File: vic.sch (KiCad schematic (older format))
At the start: 16 parts, among them U19 2016, U20 4066, U21 8564, U29 7406, U56 74LS74

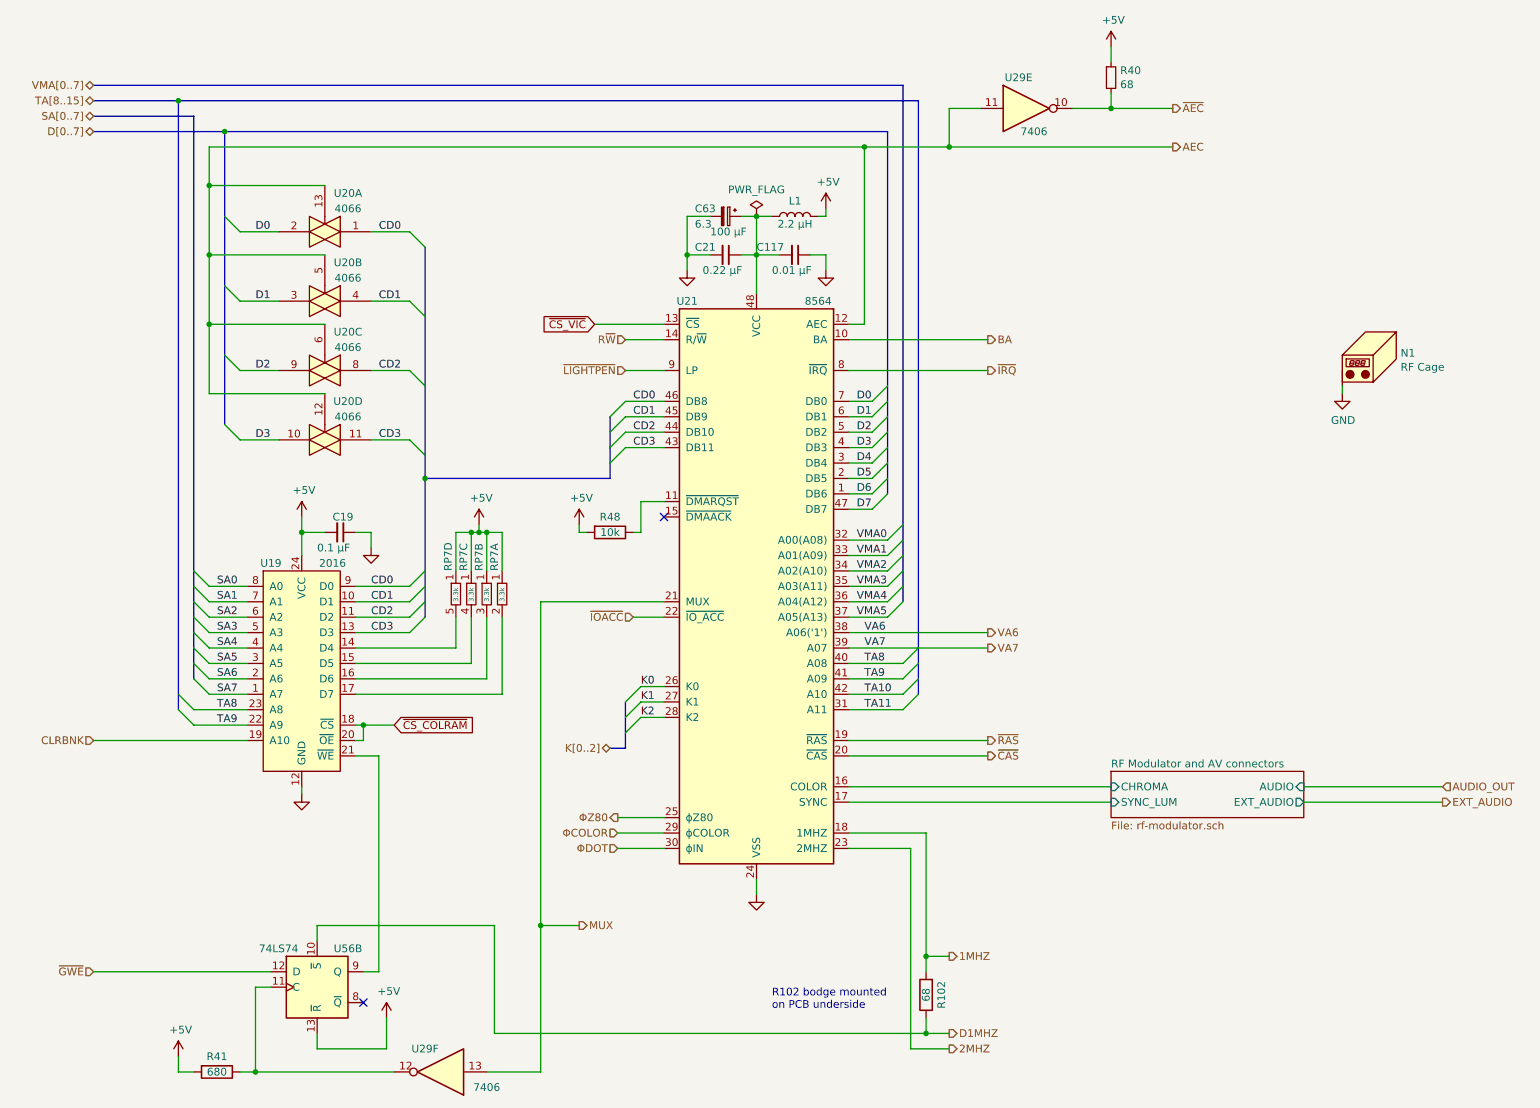
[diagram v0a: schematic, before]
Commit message: Clean up schematic
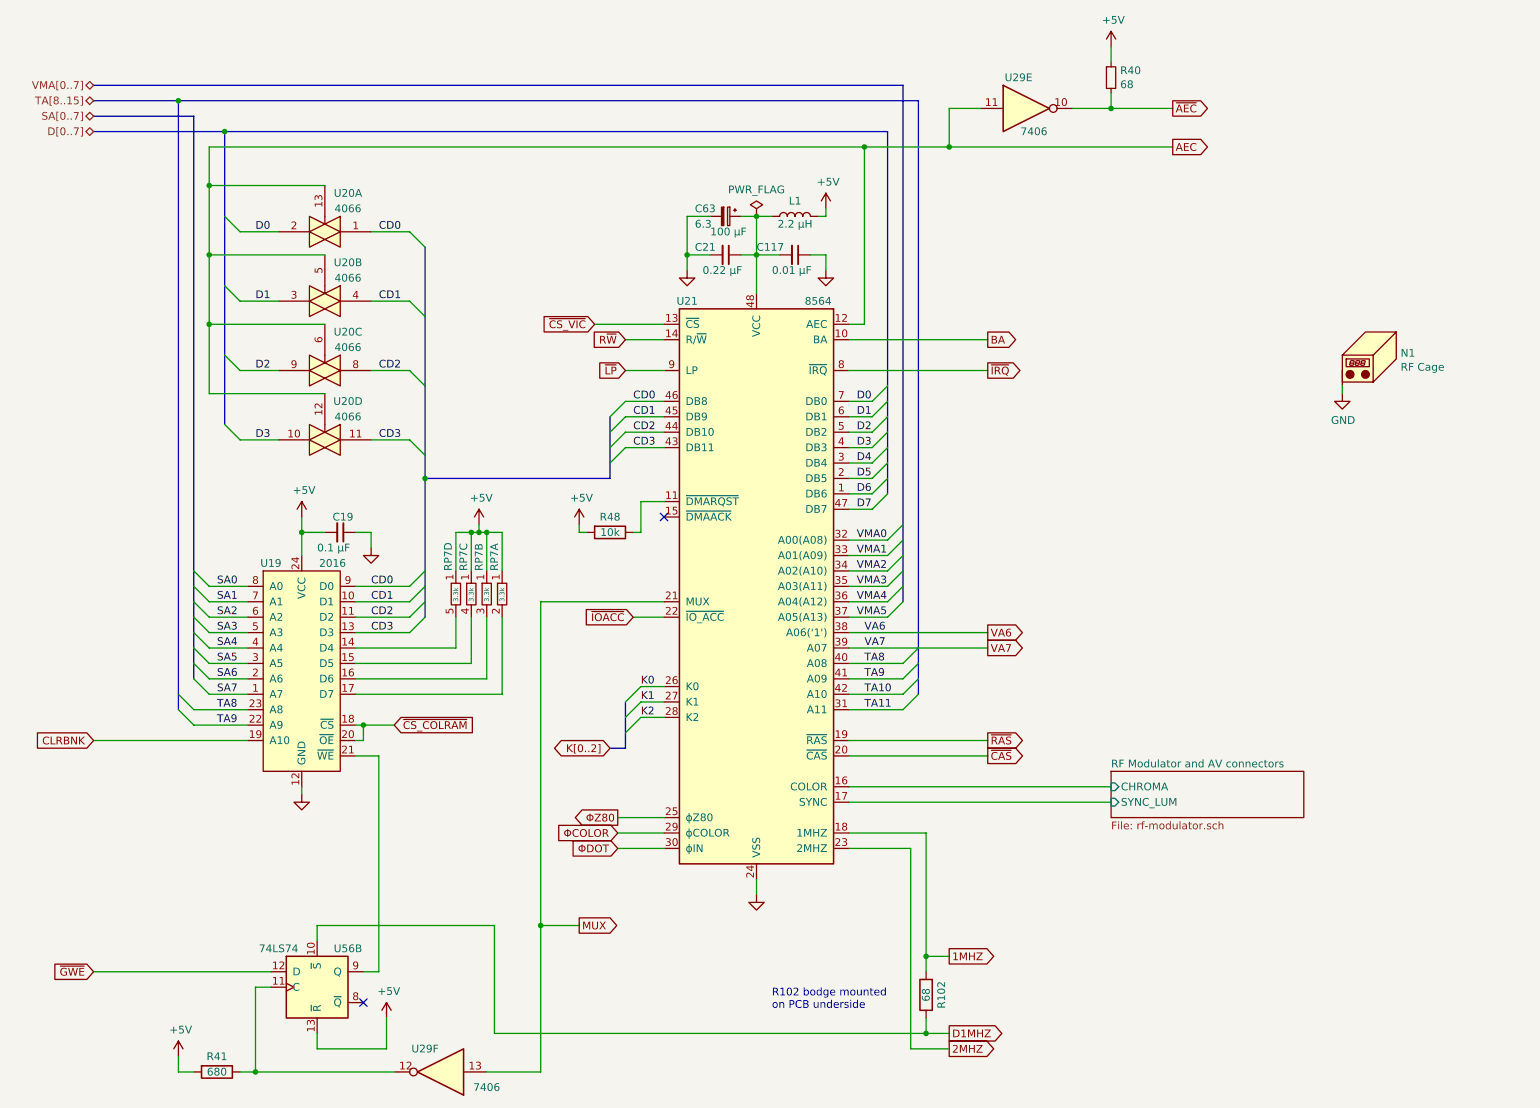
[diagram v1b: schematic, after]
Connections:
- net ~LIGHTPEN renamed ~LP
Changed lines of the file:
@@
 	1    0    0    -1
 $EndComp
-Text HLabel 4450 2850 0    50   Input ~ 0
-~LIGHTPEN
 Wire Wire Line
 	4450 2850 4700 2850
@@
 Text HLabel 1000 1300 0    50   BiDi ~ 0
 D[0..7]
-Text HLabel 6800 2650 2    50   Output ~ 0
-BA
-Text HLabel 6800 2850 2    50   Output ~ 0
-~IRQ
 Wire Wire Line
 	5900 2850 6800 2850
@@
 Wire Bus Line
 	4450 5300 4350 5300
-Text HLabel 4350 5300 0    50   BiDi ~ 0
-K[0..2]
-Text HLabel 6550 7250 2    50   Output ~ 0
-2MHZ
 Entry Wire Line
 	4350 3150 4450 3050
@@
 Text Label 1800 4950 0    50   ~ 0
 SA7
-Text HLabel 1000 5250 0    50   Input ~ 0
-CLRBNK
 Wire Wire Line
 	1000 5250 2000 5250
@@
 	1    0    0    -1
 $EndComp
-Text HLabel 8000 1400 2    50   Output ~ 0
-AEC
-Text HLabel 8000 1150 2    50   Output ~ 0
-~AEC
-Text HLabel 6800 5250 2    50   Output ~ 0
-~RAS
-Text HLabel 6800 5350 2    50   Output ~ 0
-~CAS
 Wire Wire Line
 	6800 5350 5900 5350
-Text HLabel 4400 5750 0    50   Output ~ 0
-ΦZ80
 Wire Wire Line
 	4400 5750 4700 5750
-Text HLabel 4400 5850 0    50   Input ~ 0
-ΦCOLOR
-Text HLabel 4400 5950 0    50   Input ~ 0
-ΦDOT
 Wire Wire Line
 	4400 5950 4700 5950
 Wire Wire Line
 	4400 5850 4700 5850
-Text HLabel 4450 2650 0    50   Input ~ 0
-R~W
 Wire Wire Line
 	4450 2650 4700 2650
 Wire Wire Line
 	4250 2550 4700 2550
-Text HLabel 4500 4450 0    50   Input ~ 0
-~IOACC
 Wire Wire Line
 	4500 4450 4700 4450
@@
 Wire Wire Line
 	2450 7250 2450 7150
-Text HLabel 6550 6650 2    50   Output ~ 0
-1MHZ
-Text HLabel 6550 7150 2    50   Output ~ 0
-D1MHZ
 $Comp
 L Device:R R102
@@
 Wire Wire Line
 	2450 6550 2450 6450
-Text HLabel 1000 6750 0    50   Input ~ 0
-~GWE
 Wire Wire Line
 	1000 6750 2150 6750
@@
 F0 "RF Modulator and AV connectors" 50
 F1 "rf-modulator.sch" 50
-F2 "AUDIO" I R 8850 5550 50
 F3 "SYNC_LUM" I L 7600 5650 50
 F4 "CHROMA" I L 7600 5550 50
-F5 "EXT_AUDIO" O R 8850 5650 50
 $EndSheet
 Wire Wire Line
@@
 Wire Wire Line
 	7600 5650 5900 5650
-Text HLabel 9750 5550 2    50   Input ~ 0
-AUDIO_OUT
-Text HLabel 9750 5650 2    50   Output ~ 0
-EXT_AUDIO
-Wire Wire Line
-	9750 5650 8850 5650
-Wire Wire Line
-	8850 5550 9750 5550
 Wire Wire Line
 	3900 4350 3900 6450
 Wire Wire Line
 	5900 5250 6800 5250
-Text HLabel 6800 4550 2    50   Output ~ 0
-VA6
-Text HLabel 6800 4650 2    50   Output ~ 0
-VA7
 Wire Wire Line
 	6000 1400 6550 1400
@@
 Wire Wire Line
 	3900 6450 3900 7400
-Text HLabel 4150 6450 2    50   Output ~ 0
-MUX
 Text GLabel 4250 2550 0    50   Input ~ 0
 ~CS_VIC
@@
 Wire Wire Line
 	9100 2950 9100 3000
+Text GLabel 6800 2650 2    50   Output ~ 0
+BA
+Text GLabel 6800 2850 2    50   Output ~ 0
+~IRQ
+Text GLabel 4450 2650 0    50   Input ~ 0
+R~W
+Text GLabel 8000 1150 2    50   Output ~ 0
+~AEC
+Text GLabel 8000 1400 2    50   Output ~ 0
+AEC
+Text GLabel 4400 5850 0    50   Input ~ 0
+ΦCOLOR
+Text GLabel 4400 5950 0    50   Input ~ 0
+ΦDOT
+Text GLabel 4450 2850 0    50   Input ~ 0
+~LP
+Text GLabel 1000 5250 0    50   Input ~ 0
+CLRBNK
+Text GLabel 6550 6650 2    50   Output ~ 0
+1MHZ
+Text GLabel 6550 7150 2    50   Output ~ 0
+D1MHZ
+Text GLabel 6550 7250 2    50   Output ~ 0
+2MHZ
 Wire Bus Line
 	1550 1100 1550 5050
@@
 Wire Bus Line
 	6150 1300 6150 3650
+Text GLabel 4400 5750 0    50   Output ~ 0
+ΦZ80
+Text GLabel 4150 6450 2    50   Output ~ 0
+MUX
+Text GLabel 6800 5250 2    50   Output ~ 0
+~RAS
+Text GLabel 6800 5350 2    50   Output ~ 0
+~CAS
+Text GLabel 6800 4550 2    50   Output ~ 0
+VA6
+Text GLabel 6800 4650 2    50   Output ~ 0
+VA7
+Text GLabel 1000 6750 0    50   Input ~ 0
+~GWE
+Text GLabel 4500 4450 0    50   Input ~ 0
+~IOACC
+Text GLabel 4350 5300 0    50   BiDi ~ 0
+K[0..2]
 $EndSCHEMATC
